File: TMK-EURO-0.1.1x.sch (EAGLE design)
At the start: 55 parts, among them IC1 TL082P, U1 IN, U2 IN, U3 IN, U4 IN, U5 IN, U6 IN, U7 THONKICONNOLD, X1 057-010-1

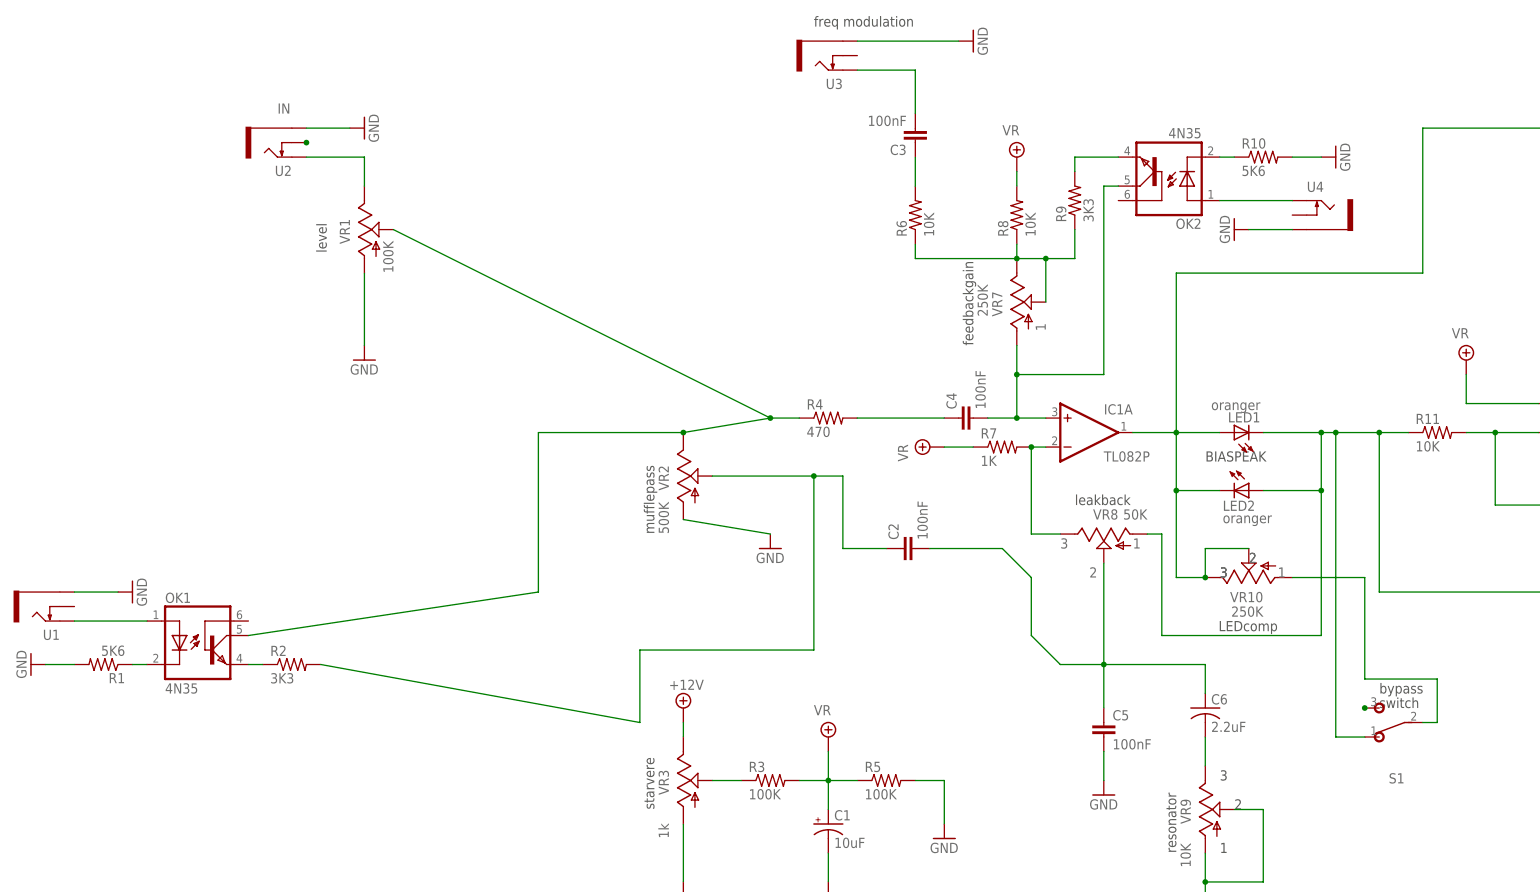
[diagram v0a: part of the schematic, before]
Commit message: Cleanup for errors
Removed all the CV-inputs. Fixed the power. Check this on breadboard
first!
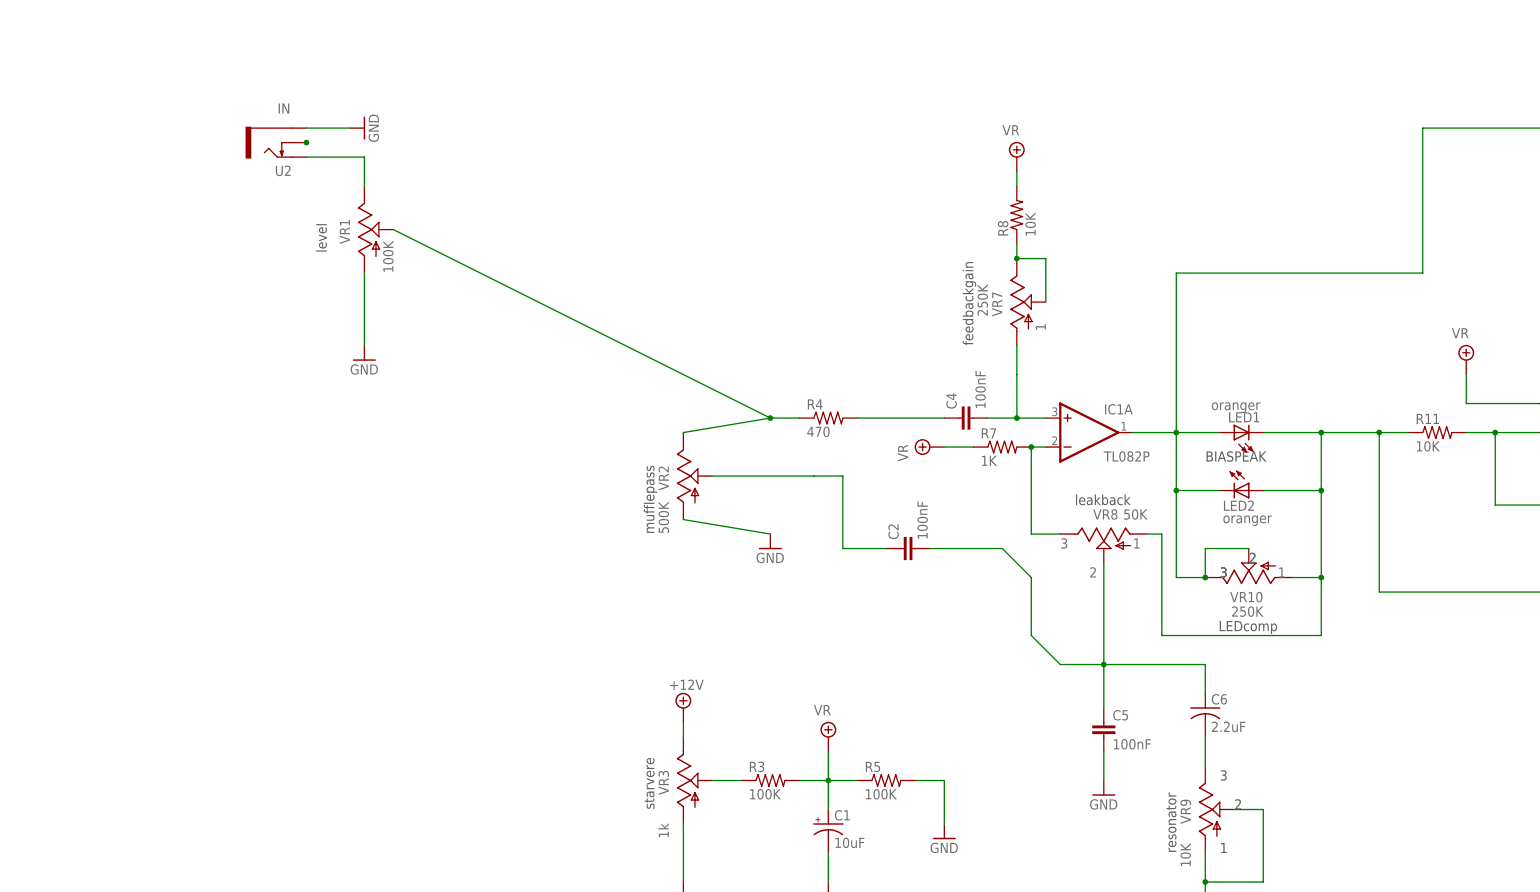
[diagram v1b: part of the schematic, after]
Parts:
- removed C3: 100nF, rcl:C-EU050-035X075
- removed OK1, OK2: 4N35, optocoupler:4N35
- removed R1, R10: 5K6, adafruit:R-US_0207/7
- removed R2, R9: 3K3, adafruit:R-US_0207/7
- removed R6: 10K, adafruit:R-US_0207/7
- removed S1: (no value), momentswitchREDlveewrergalmoer mini switch:SPDTPADS
- removed U1, U3, U4: IN, MusicThingModular:THONKICONNOLD
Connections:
- removed net BYPASS: S1.P, VR10.A
- removed net N$27: OK2.EMI, R9.2
- removed net N$28: OK2.C, R10.1
- removed net N$30: OK2.A, U4.TIP
- removed net N$31: OK1.EMI, R2.1
- removed net N$32: OK1.C, R1.1
- removed net N$33: OK1.A, U1.TIP
- removed net N$34: S1.S
- removed net N$36: C3.1, R6.2
- removed net N$37: C3.2, U3.TIP
- removed net N$4: C4.2, IC1A.+IN, OK2.COL, VR7.A
- new net N$26: C4.2, IC1A.+IN, VR7.A
- net GND: no longer R1.2, R10.2, U1.SLEEVE, U3.SLEEVE, U4.SLEEVE
- net N$2: no longer OK1.COL
- net N$5: no longer R6.1, R9.1
- net N$7: now also VR10.A; no longer S1.O
- net N$9: no longer R2.2
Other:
- note removed: "bypass"
- note removed: "freq modulation"
- note removed: "switch"

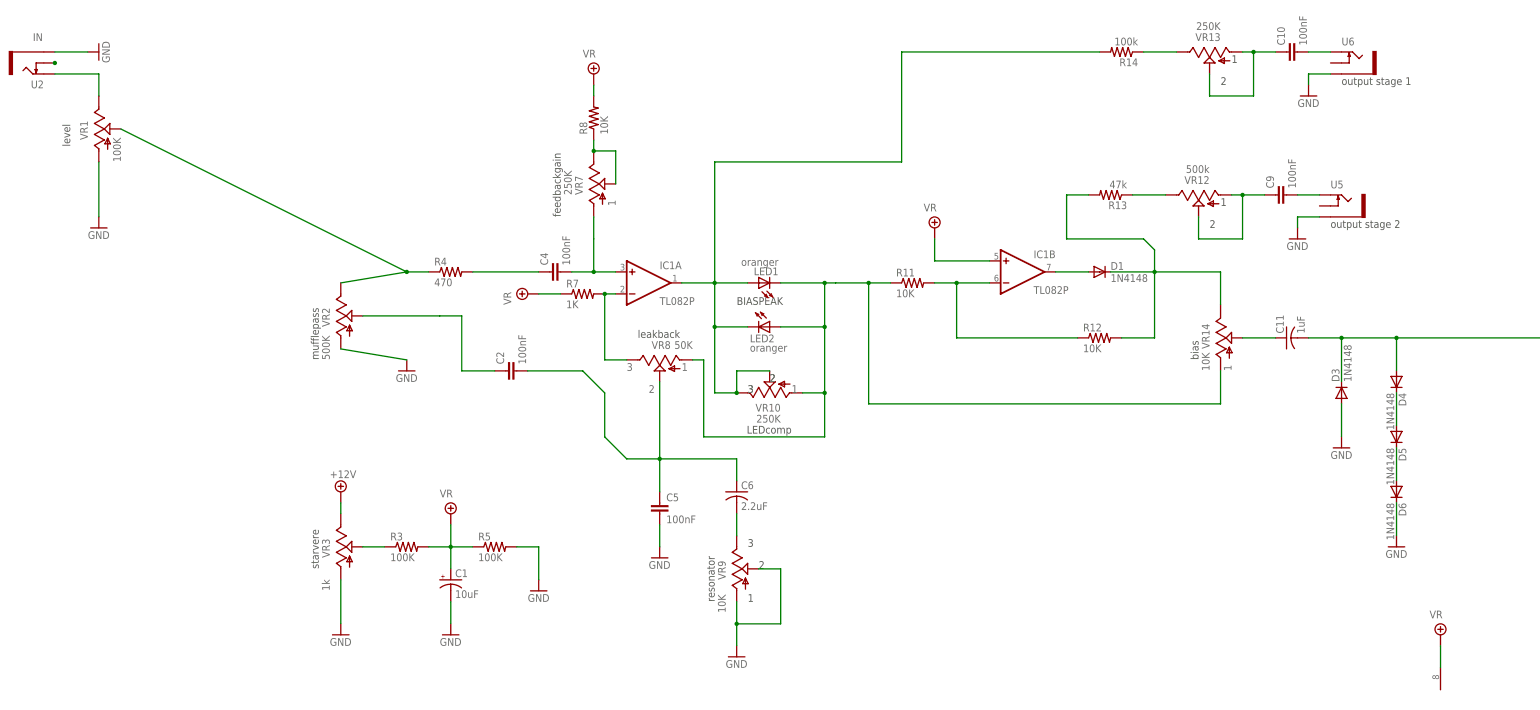
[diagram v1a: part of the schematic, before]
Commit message: Fixed power
No Vr on power pin 8, but 12V from the main power supply
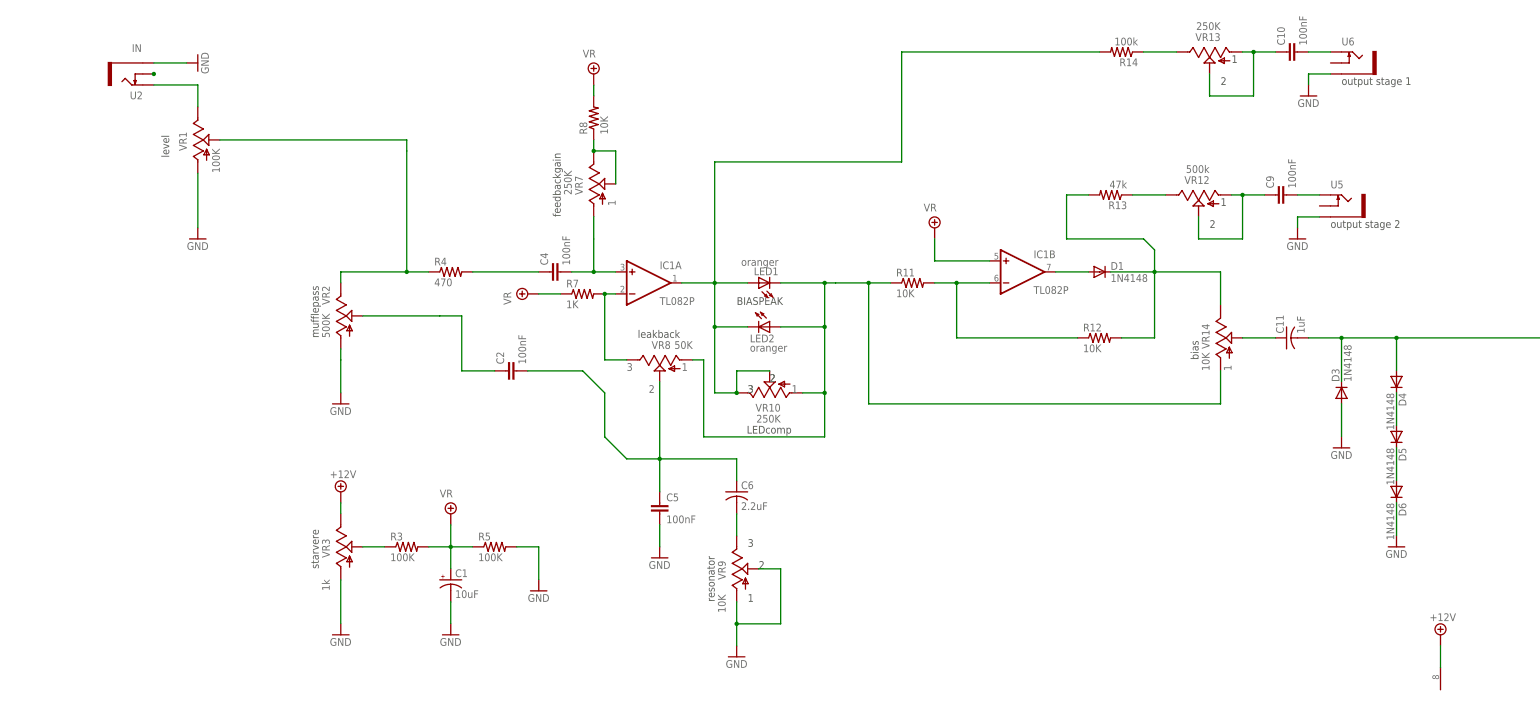
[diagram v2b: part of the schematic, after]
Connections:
- net +12V: now also IC1P.V+
- net VR: no longer IC1P.V+
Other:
- moved on the sheet: U2, VR1
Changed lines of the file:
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@@
 <part name="VR4" library="gm-supply" deviceset="VR" device=""/>
 <part name="GND21" library="supply1" deviceset="GND" device=""/>
-<part name="VR15" library="gm-supply" deviceset="VR" device=""/>
 <part name="GND19" library="supply1" deviceset="GND" device=""/>
 <part name="GND20" library="supply1" deviceset="GND" device=""/>
@@
 <part name="SUPPLY3" library="supply2" deviceset="+12V" device=""/>
 <part name="GND27" library="supply1" deviceset="GND" device=""/>
+<part name="SUPPLY2" library="supply2" deviceset="+12V" device=""/>
 </parts>
 <sheets>
 <sheet>
 <plain>
-<text x="-50.8" y="170.18" size="1.778" layer="95">IN</text>
+<text x="-27.94" y="167.64" size="1.778" layer="95">IN</text>
 <text x="124.46" y="88.9" size="1.778" layer="96">1</text>
 <text x="119.38" y="91.44" size="1.778" layer="96">2</text>
@@
 <text x="226.06" y="93.98" size="1.778" layer="96" rot="R90">1</text>
 <text x="332.74" y="78.74" size="1.778" layer="95">OUT</text>
-<text x="-42.164" y="145.796" size="1.778" layer="97" rot="R90">level</text>
+<text x="-19.304" y="143.256" size="1.778" layer="97" rot="R90">level</text>
 <text x="71.12" y="129.54" size="1.778" layer="97" rot="R90">feedbackgain </text>
 <text x="15.24" y="48.26" size="1.778" layer="97" rot="R90">starvere</text>
 <text x="124.46" y="81.28" size="1.778" layer="97" rot="R180">LEDcomp</text>
-<text x="15.24" y="96.52" size="1.778" layer="97" rot="R90">mufflepass</text>
+<text x="15.24" y="101.6" size="1.778" layer="97" rot="R90">mufflepass</text>
 <text x="88.9" y="101.6" size="1.778" layer="97">leakback</text>
 <text x="111.76" y="109.22" size="1.778" layer="97">BIASPEAK</text>
@@
 <instance part="R3" gate="G$1" x="35.56" y="53.34"/>
 <instance part="R5" gate="G$1" x="55.88" y="53.34"/>
-<instance part="VR1" gate="G$1" x="-35.56" y="149.86" smashed="yes">
-<attribute name="NAME" x="-38.1" y="147.32" size="1.778" layer="95" rot="R90"/>
-<attribute name="VALUE" x="-30.48" y="142.24" size="1.778" layer="96" rot="R90"/>
+<instance part="VR1" gate="G$1" x="-12.7" y="147.32" smashed="yes">
+<attribute name="NAME" x="-15.24" y="144.78" size="1.778" layer="95" rot="R90"/>
+<attribute name="VALUE" x="-7.62" y="139.7" size="1.778" layer="96" rot="R90"/>
 </instance>
 <instance part="VR2" gate="G$1" x="20.32" y="106.68" smashed="yes">
-<attribute name="NAME" x="17.78" y="104.14" size="1.778" layer="95" rot="R90"/>
-<attribute name="VALUE" x="17.78" y="96.52" size="1.778" layer="96" rot="R90"/>
+<attribute name="NAME" x="17.78" y="109.22" size="1.778" layer="95" rot="R90"/>
+<attribute name="VALUE" x="17.78" y="101.6" size="1.778" layer="96" rot="R90"/>
 </instance>
 <instance part="VR7" gate="G$1" x="78.74" y="137.16" smashed="yes">
@@
 <instance part="D5" gate="G$1" x="264.16" y="78.74" rot="R270"/>
 <instance part="D6" gate="G$1" x="264.16" y="66.04" rot="R270"/>
-<instance part="U2" gate="G$1" x="-50.8" y="165.1" rot="R180"/>
+<instance part="U2" gate="G$1" x="-27.94" y="162.56" rot="R180"/>
 <instance part="U7" gate="G$1" x="335.28" y="86.36"/>
 <instance part="C1" gate="G$1" x="45.72" y="45.72"/>
@@
 <instance part="C6" gate="G$1" x="111.76" y="66.04"/>
 <instance part="IC1" gate="P" x="274.32" y="17.78"/>
-<instance part="GND3" gate="1" x="-35.56" y="167.64" rot="R90"/>
-<instance part="GND4" gate="1" x="-35.56" y="127"/>
-<instance part="GND6" gate="1" x="35.56" y="93.98"/>
+<instance part="GND3" gate="1" x="-12.7" y="165.1" rot="R90"/>
+<instance part="GND4" gate="1" x="-12.7" y="124.46"/>
+<instance part="GND6" gate="1" x="20.32" y="86.36"/>
 <instance part="VR6" gate="G$1" x="78.74" y="162.56"/>
 <instance part="VR5" gate="G$1" x="63.5" y="111.76" rot="R90"/>
@@
 <instance part="VR4" gate="G$1" x="45.72" y="60.96"/>
 <instance part="GND21" gate="1" x="274.32" y="2.54"/>
-<instance part="VR15" gate="G$1" x="274.32" y="33.02"/>
 <instance part="GND19" gate="1" x="251.46" y="76.2"/>
 <instance part="GND20" gate="1" x="264.16" y="53.34"/>
@@
 <instance part="SUPPLY3" gate="+12V" x="289.56" y="-12.7"/>
 <instance part="GND27" gate="1" x="162.56" y="-17.78" rot="R270"/>
+<instance part="SUPPLY2" gate="+12V" x="274.32" y="33.02"/>
 </instances>
 <busses>
@@
 <segment>
 <pinref part="VR1" gate="G$1" pin="E"/>
-<wire x1="-35.56" y1="157.48" x2="-35.56" y2="162.56" width="0.1524" layer="91"/>
-<wire x1="-35.56" y1="162.56" x2="-45.72" y2="162.56" width="0.1524" layer="91"/>
+<wire x1="-12.7" y1="154.94" x2="-12.7" y2="160.02" width="0.1524" layer="91"/>
+<wire x1="-12.7" y1="160.02" x2="-22.86" y2="160.02" width="0.1524" layer="91"/>
 <pinref part="U2" gate="G$1" pin="TIP"/>
 </segment>
@@
 <segment>
 <pinref part="U2" gate="G$1" pin="SWITCH"/>
-<junction x="-45.72" y="165.1"/>
+<junction x="-22.86" y="162.56"/>
 </segment>
 </net>
@@
 <pinref part="U2" gate="G$1" pin="SLEEVE"/>
 <pinref part="GND3" gate="1" pin="GND"/>
-<wire x1="-45.72" y1="167.64" x2="-38.1" y2="167.64" width="0.1524" layer="91"/>
+<wire x1="-22.86" y1="165.1" x2="-15.24" y2="165.1" width="0.1524" layer="91"/>
 </segment>
 <segment>
 <pinref part="GND4" gate="1" pin="GND"/>
 <pinref part="VR1" gate="G$1" pin="A"/>
-<wire x1="-35.56" y1="129.54" x2="-35.56" y2="142.24" width="0.1524" layer="91"/>
+<wire x1="-12.7" y1="127" x2="-12.7" y2="139.7" width="0.1524" layer="91"/>
 </segment>
 <segment>
 <pinref part="VR2" gate="G$1" pin="A"/>
 <pinref part="GND6" gate="1" pin="GND"/>
-<wire x1="20.32" y1="99.06" x2="35.56" y2="96.52" width="0.1524" layer="91"/>
+<wire x1="20.32" y1="99.06" x2="20.32" y2="96.52" width="0.1524" layer="91"/>
+<wire x1="20.32" y1="96.52" x2="20.32" y2="88.9" width="0.1524" layer="91"/>
 </segment>
 <segment>
@@
 <pinref part="VR1" gate="G$1" pin="S"/>
 <pinref part="R4" gate="G$1" pin="1"/>
-<wire x1="-30.48" y1="149.86" x2="35.56" y2="116.84" width="0.1524" layer="91"/>
+<wire x1="-7.62" y1="147.32" x2="35.56" y2="147.32" width="0.1524" layer="91"/>
+<wire x1="35.56" y1="147.32" x2="35.56" y2="144.78" width="0.1524" layer="91"/>
+<wire x1="35.56" y1="144.78" x2="35.56" y2="116.84" width="0.1524" layer="91"/>
 <pinref part="VR2" gate="G$1" pin="E"/>
 <wire x1="35.56" y1="116.84" x2="40.64" y2="116.84" width="0.1524" layer="91"/>
-<wire x1="20.32" y1="114.3" x2="35.56" y2="116.84" width="0.1524" layer="91"/>
+<wire x1="20.32" y1="114.3" x2="20.32" y2="116.84" width="0.1524" layer="91"/>
+<wire x1="20.32" y1="116.84" x2="35.56" y2="116.84" width="0.1524" layer="91"/>
 <junction x="35.56" y="116.84"/>
 </segment>
@@
 <pinref part="VR4" gate="G$1" pin="VR"/>
 <junction x="45.72" y="53.34"/>
-</segment>
-<segment>
-<pinref part="VR15" gate="G$1" pin="VR"/>
-<pinref part="IC1" gate="P" pin="V+"/>
-<wire x1="274.32" y1="30.48" x2="274.32" y2="25.4" width="0.1524" layer="91"/>
 </segment>
 </net>
@@
 <pinref part="SUPPLY3" gate="+12V" pin="+12V"/>
 </segment>
-</net>
+<segment>
+<pinref part="IC1" gate="P" pin="V+"/>
+<wire x1="274.32" y1="30.48" x2="274.32" y2="25.4" width="0.1524" layer="91"/>
+<pinref part="SUPPLY2" gate="+12V" pin="+12V"/>
+</segment>
+</net>
